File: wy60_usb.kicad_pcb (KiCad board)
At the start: 2 copper layers, 407.9 x 170.4 mm, 223 parts, among them J1 AVR-ISP-6, U1 ATmega32A-PU

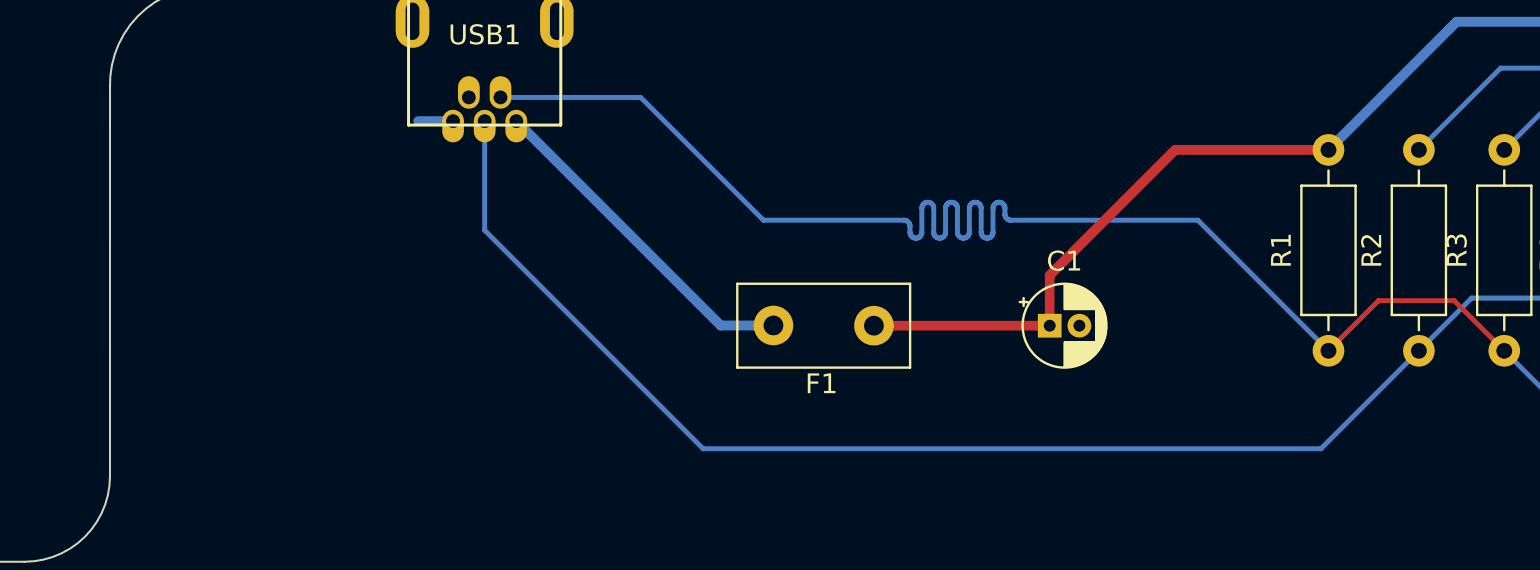
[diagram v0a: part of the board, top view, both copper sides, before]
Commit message: added JST port for fixed cable
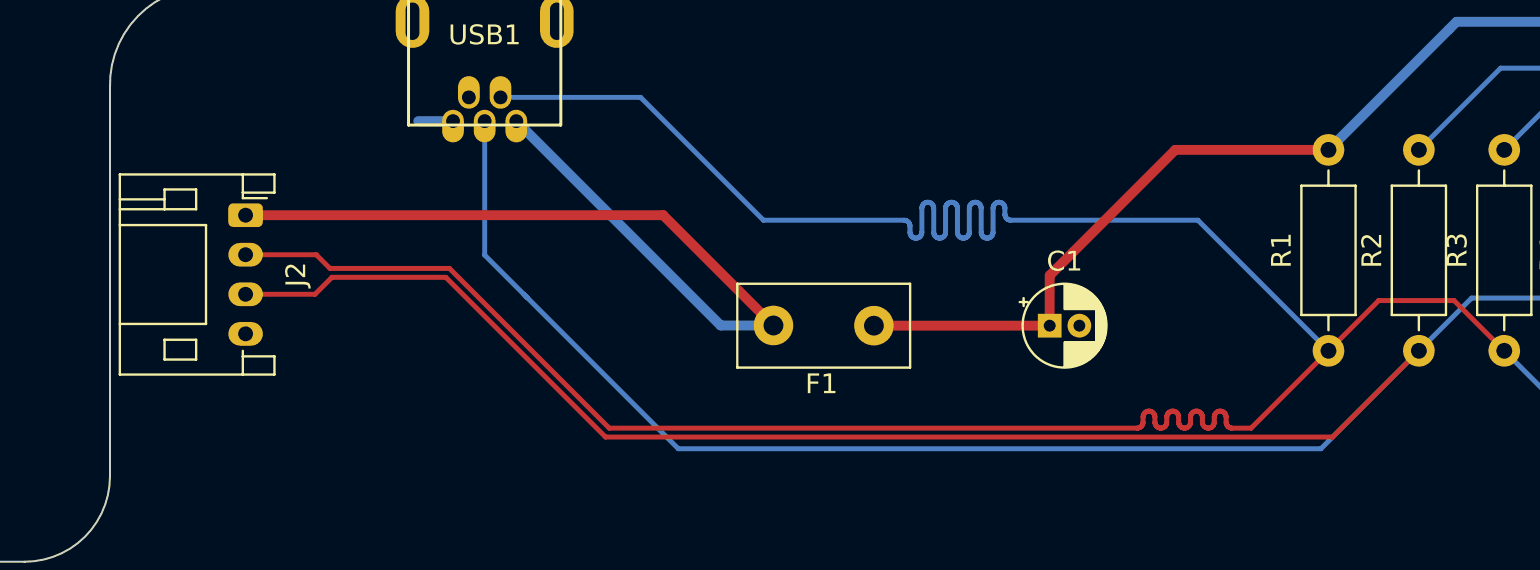
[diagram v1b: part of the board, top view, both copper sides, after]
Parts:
- added J2: Conn_01x04, Connector_JST:JST_PH_S4B-PH-K_1x04_P2.00mm_Horizontal, F.Cu at (31.9, 61.7)
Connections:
- net Net-(D1-Pad1) renamed D+RAW
- net Net-(D2-Pad1) renamed D-RAW
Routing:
- net D+RAW: track 69.9 -> 135.7 mm
- net D-RAW: track 80.6 -> 145.5 mm
- net VCC: track 17.3 -> 46.3 mm

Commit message: add jst legends
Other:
- board text added: "D+"
- board text added: "D-"
- board text added: "GND"
- board text added: "VCC"
